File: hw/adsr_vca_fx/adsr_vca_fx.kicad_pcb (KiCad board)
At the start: 4 copper layers, 87 x 89.5 mm, 110 parts, among them J1 Conn_01x03, J10 VCA2 Extern, J11 Conn_01x04, J2 Conn_02x02_Odd_Even, J3 Conn_02x02_Odd_Even, J4 Audio Input, J5 Audio Output, J6 Conn_02x05_Odd_Even, J7 Envelope2 Extern, J8 Envelope1 Extern, J9 VCA1 Extern, Q1 HX2301A, SW1 SW_Push, U1 TL972, U2 MCP603-xCH, U3 STM32L432KBUx, U4 LM13700, U5 TL972, U6 TPS563200, U7 SE8233X2, U8 TPS60403, U9 TPS60403

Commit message: tidied up layout
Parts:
- removed JP2: SolderJumper_3_Bridged12, Jumper:SolderJumper-3_P1.3mm_Bridged12_Pad1.0x1.5mm
- added J12: Conn_01x03, Connector_PinHeader_2.54mm:PinHeader_1x03_P2.54mm_Vertical, F.Cu at (175.9, 78.1)
- JP1: footprint Connector_PinSocket_2.54mm:PinSocket_1x02_P2.54mm_Vertical -> Connector_PinHeader_2.54mm:PinHeader_1x02_P2.54mm_Vertical
- moved J4 18.7 mm to (146.6, 129.7), turned to 90 degrees
- moved RV4 12.6 mm to (192.3, 121.1), turned to -90 degrees
- moved RV14 12.5 mm to (123.2, 136.5), turned to -90 degrees
- moved RV11 12.5 mm to (123.2, 85.1), turned to -90 degrees
- moved RV12 12.5 mm to (123.2, 119.4), turned to -90 degrees
- moved RV13 12.5 mm to (123.2, 102.2), turned to -90 degrees
- moved RV2 12.5 mm to (192.3, 85.6), turned to -90 degrees
- moved RV3 12.5 mm to (192.3, 103.2), turned to -90 degrees
- moved R2 11.6 mm to (189.7, 91.9)
- moved R6 9.85 mm to (175.9, 81.3)
- moved TP5 7.67 mm to (142.2, 104.8)
- moved J7 6.66 mm to (134.6, 105.2), turned to 90 degrees
- moved TP8 5.84 mm to (163.0, 143.0)
- moved R4 5.04 mm to (188.8, 124.0), turned to 180 degrees
- moved J8 4.30 mm to (177.8, 105.4)
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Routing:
- net +3.3V: track 278.8 -> 251.3 mm, vias 9 -> 8
- net /AudioOutput/audio_in1: track 47.2 -> 63.8 mm
- net /AudioOutput/audio_in2: track 44.4 -> 57.6 mm
- net Net-(R3-Pad1): track 2.67 -> 12.5 mm
- net /AudioInput/audio_out: track 66.5 -> 75.8 mm
- net /ADSRPots/env_in.decay: track 62.6 -> 53.6 mm
- net /ADSRPots/env_in.attack: track 48.6 -> 39.7 mm
- net /ADSRPots/env_in.sustain: track 77.7 -> 69.0 mm
- net /ADSRPots/env_in.release: track 93.6 -> 85.2 mm
- net /EnvelopeGenerator/boot0: track 10.8 -> 18.8 mm, vias 1 -> 0
- net Net-(J4-Pin_2): track 28.4 -> 36.3 mm
- net Net-(U4C--): track 27.4 -> 22.8 mm
- net Net-(U1B--): track 65.4 -> 69.9 mm
- net /EnvelopeGenerator/reset: track 39.3 -> 43.4 mm
- net Net-(J8-Pin_2): track 37.5 -> 34.1 mm
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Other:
- board text removed: "+12V"
- board text removed: "+5V"
- board text removed: "-5V"
- board text removed: "DETECT"
- board text removed: "INPUT"
- board text removed: "INPUT GAIN"
- board text removed: "OUTPUT"
- board text removed: "PEAK"
- board text removed: "VCA1"
- board text removed: "VCA1 ENV OUT"
- board text removed: "VCA1 GAIN"
- board text removed: "VCA1 OFFSET"
- board text removed: "VCA2"
- board text removed: "VCA2 ENV OUT"
- board text removed: "VCA2 GAIN"
- board text removed: "VCA2 OFFSET"

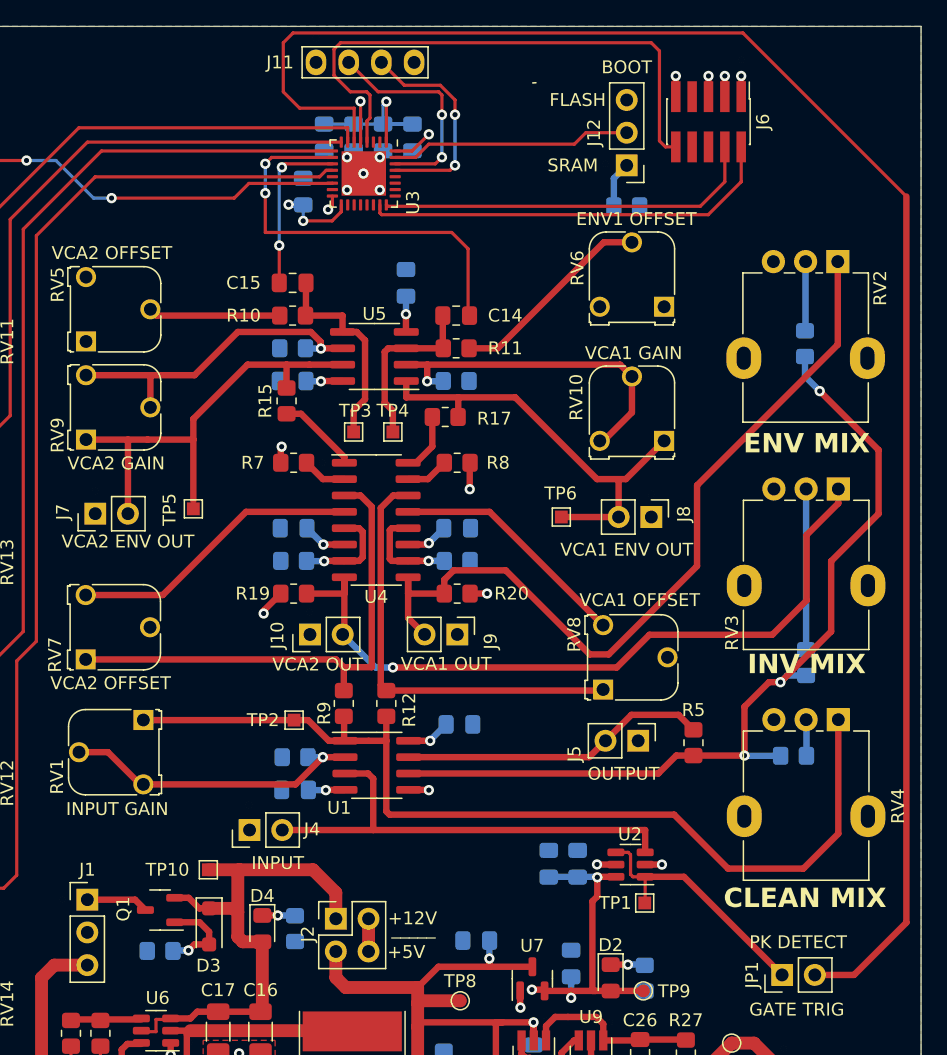
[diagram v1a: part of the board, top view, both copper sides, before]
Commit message: updated layout
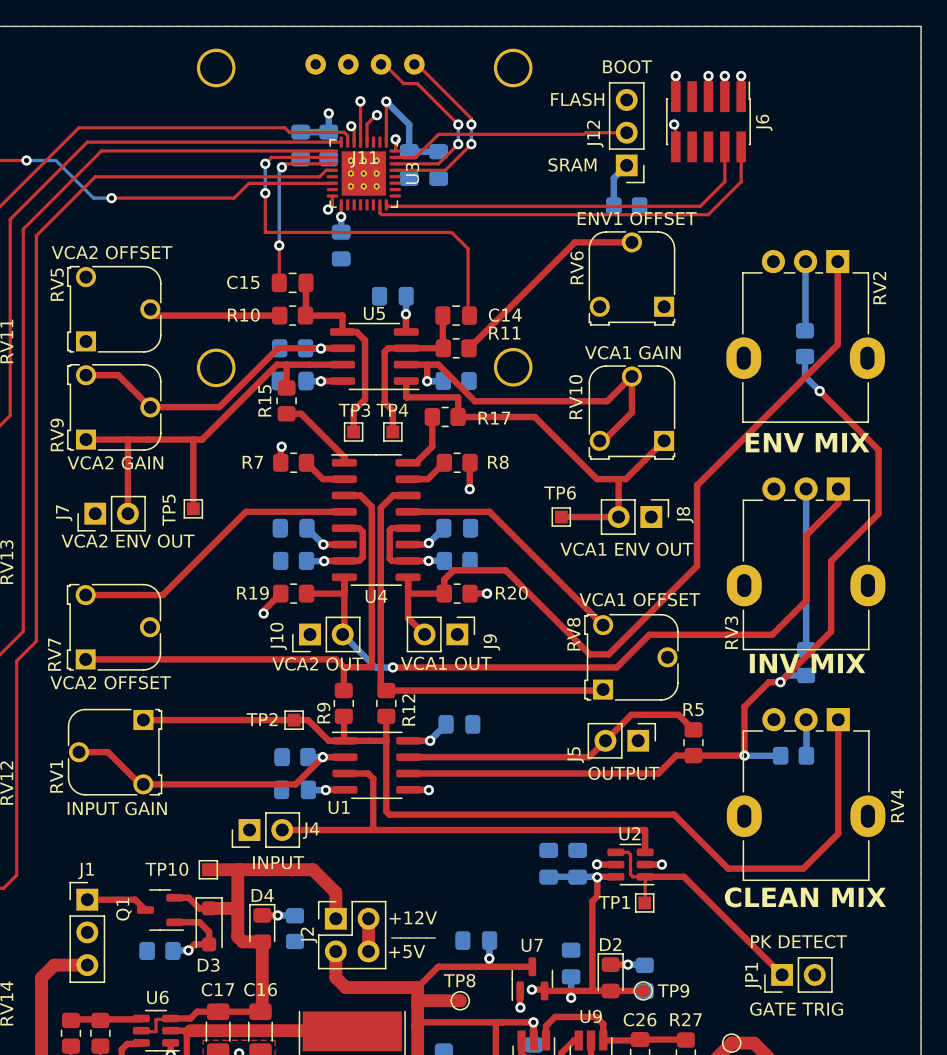
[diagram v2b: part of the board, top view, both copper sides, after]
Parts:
- J11: footprint 128x64_0_96InchOLED:128x64_0_96InchOLED -> SSD1306_0.96_Oled:SSD1306_0.96_Oled_no_courtyard_no_silkscreen
- U3: footprint Package_DFN_QFN:QFN-32-1EP_5x5mm_P0.5mm_EP3.45x3.45mm -> Package_DFN_QFN:QFN-32-1EP_5x5mm_P0.5mm_EP3.45x3.45mm_ThermalVias
- moved J11 18.8 mm to (142.6, 94.5)
- moved C7 9.15 mm to (161.3, 78.1)
- moved C8 6.53 mm to (152.8, 76.6)
- moved C9 6.43 mm to (150.6, 76.6)
- moved C6 5.13 mm to (153.7, 84.3), turned to -90 degrees
- moved C5 4.82 mm to (159.0, 78.1)
- moved C13 1.45 mm to (157.7, 88.3), turned to 0 degrees
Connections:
- J11 pad 2: /EnvelopeGenerator/displaybus.sda -> +3.3V
- J11 pad 3: /EnvelopeGenerator/displaybus.scl -> /EnvelopeGenerator/displaybus.sda
- J11 pad 4: +3.3V -> /EnvelopeGenerator/displaybus.scl
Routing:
- net /EnvelopeGenerator/peak_detect_gatecv: track 131.6 -> 91.6 mm, vias 0 -> 1
- net /EnvelopeGenerator/reset: track 43.4 -> 27.6 mm, vias 0 -> 2
- net +3.3V: track 251.3 -> 260.4 mm
- net VDDA: track 147.5 -> 144.2 mm
- net GND: track 36.2 -> 33.9 mm, vias 23 -> 18
- net /EnvelopeGenerator/displaybus.sda: track 17.0 -> 15.0 mm
- net /EnvelopeGenerator/displaybus.scl: track 16.8 -> 15.0 mm
- net Net-(U5B--): track 25.8 -> 24.0 mm
- net Net-(U5A--): track 26.7 -> 28.3 mm
- net Net-(J7-Pin_2): track 35.6 -> 34.6 mm
- net Net-(J8-Pin_2): track 34.1 -> 33.4 mm

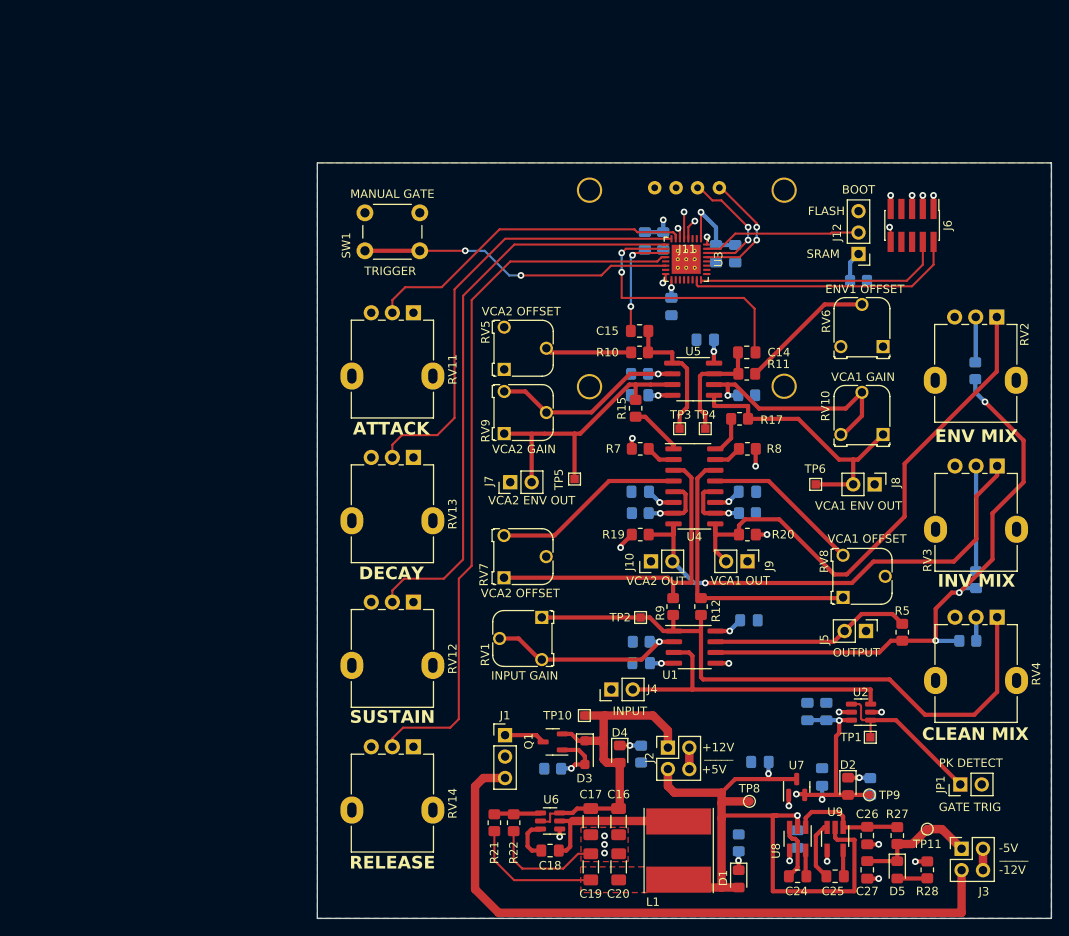
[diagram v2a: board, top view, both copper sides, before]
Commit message: updated layout
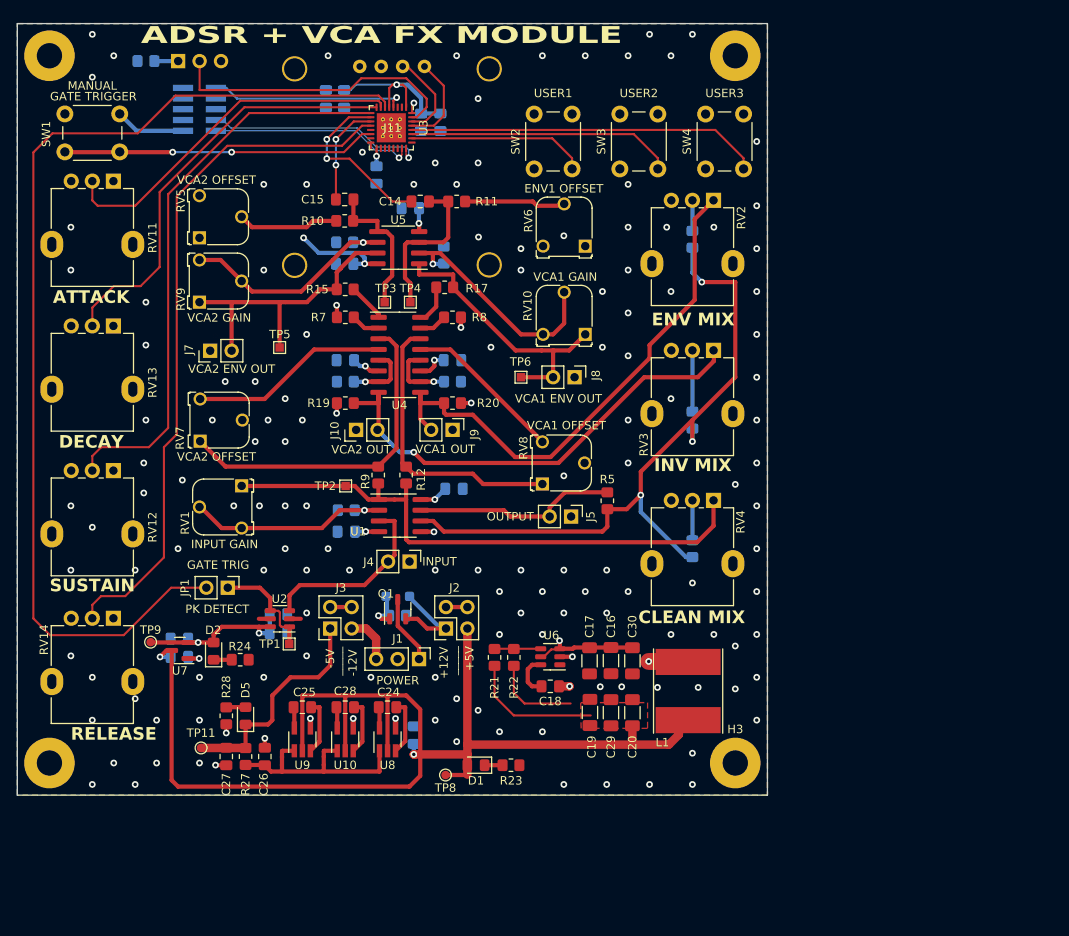
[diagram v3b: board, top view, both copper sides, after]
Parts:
- removed D4: RED, LED_SMD:LED_0805_2012Metric_Pad1.15x1.40mm_HandSolder
- removed R26: 2K2, Resistor_SMD:R_0805_2012Metric_Pad1.20x1.40mm_HandSolder
- removed TP10: TestPoint, TestPoint:TestPoint_Pad_1.0x1.0mm
- added C28: 1uf, Capacitor_SMD:C_0805_2012Metric_Pad1.18x1.45mm_HandSolder, F.Cu at (115.1, 131.8)
- added C29: 22uF, Resistor_SMD:R_1206_3216Metric_Pad1.30x1.75mm_HandSolder, F.Cu at (146.6, 132.5)
- added C30: 100nF, Resistor_SMD:R_1206_3216Metric_Pad1.30x1.75mm_HandSolder, F.Cu at (149.1, 126.3)
- added H1: MountingHole, MountingHole:MountingHole_3mm_Pad, F.Cu at (161.3, 54.6)
- added H2: MountingHole, MountingHole:MountingHole_3mm_Pad, F.Cu at (80.0, 54.6)
- added H3: MountingHole, MountingHole:MountingHole_3mm_Pad, F.Cu at (161.3, 138.4)
- added H4: MountingHole, MountingHole:MountingHole_3mm_Pad, F.Cu at (80.0, 138.4)
- added NT2: NetTie_2, NetTie:NetTie-2_SMD_Pad0.5mm, F.Cu at (107.6, 138.2)
- added SW2: SW_Push, Button_Switch_THT:SW_PUSH_6mm, F.Cu at (137.4, 68.0)
- added SW3: SW_Push, Button_Switch_THT:SW_PUSH_6mm, F.Cu at (147.6, 68.0)
- added SW4: SW_Push, Button_Switch_THT:SW_PUSH_6mm, F.Cu at (157.8, 68.0)
- added U10: TPS60403, Package_TO_SOT_SMD:SOT-23-5_HandSoldering, F.Cu at (115.1, 135.6)
- C16, C17: value 10uF 20V X5R -> 10uF
- C19, C20: value 22uF 10V X5R -> 22uF
- D3, J12, J6: moved to B.Cu
- R23, R24: moved to F.Cu
- moved JP1 89.9 mm to (101.1, 117.7), turned to -90 degrees
- moved R6 88.4 mm to (91.4, 55.2), turned to 180 degrees
- moved TP9 87.1 mm to (92.0, 124.1), turned to 0 degrees
- moved TP11 86.6 mm to (98.0, 136.6), turned to 180 degrees
- moved J6 85.6 mm to (97.8, 61.0), turned to 0 degrees
- moved R28 85.1 mm to (101.0, 132.8), turned to -90 degrees
- moved J12 83.8 mm to (95.3, 55.2), turned to -90 degrees
- moved D5 79.4 mm to (103.3, 132.8), turned to 90 degrees
- moved J3 79.2 mm to (113.3, 122.5), turned to 90 degrees
- moved C22 77.9 mm to (95.4, 123.7), turned to 180 degrees
- moved R27 77.8 mm to (103.3, 137.7), turned to 90 degrees
- moved C27 77.1 mm to (101.0, 137.7)
- moved D2 76.9 mm to (99.5, 125.2), turned to 90 degrees
- moved R24 76.2 mm to (102.6, 126.2), turned to 0 degrees
- moved U7 74.9 mm to (95.5, 125.1), turned to 180 degrees
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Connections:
- C26 pad 1: Net-(U9-OUT) -> Net-(U8-OUT)
- NT1 pad 1: Net-(U8-OUT) -> Net-(U10-OUT)
- NT1 pad 2: Net-(U9-OUT) -> Net-(U8-OUT)
- R27 pad 1: Net-(U9-OUT) -> Net-(U8-OUT)
- U3 pad 26: unconnected-(U3-PB3-Pad26) -> /EnvelopeGenerator/user_btn1
- U3 pad 27: unconnected-(U3-PB4-Pad27) -> /EnvelopeGenerator/user_btn2
- U3 pad 28: unconnected-(U3-PB5-Pad28) -> /EnvelopeGenerator/user_btn3
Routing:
- net VSSA: track 231.1 -> 134.3 mm
- net VSS: track 80.0 -> 5.83 mm
- net /PowerSupply/+5V: track 100.6 -> 165.0 mm
- net /EnvelopeGenerator/user_btn3: track 0.00 -> 48.5 mm
- net /EnvelopeGenerator/user_btn2: track 0.00 -> 38.1 mm
- net /EnvelopeGenerator/peak_detect_gatecv: track 91.6 -> 124.3 mm, vias 1 -> 0
- net /EnvelopeGenerator/user_btn1: track 0.00 -> 27.7 mm
- net Net-(U8-OUT): track 2.12 -> 20.2 mm
- net /EnvelopeGenerator/boot0: track 18.8 -> 35.2 mm
- net VDDA: track 144.2 -> 129.9 mm, vias 5 -> 6
- net Net-(J4-Pin_2): track 36.3 -> 22.1 mm
- net Net-(U1B--): track 69.9 -> 82.4 mm
- net +3.3V: track 260.4 -> 272.8 mm, vias 8 -> 4
- net /PowerSupply/-5V: track 14.9 -> 27.2 mm
- net /EnvelopeGenerator/adsr_env_out1: track 32.3 -> 20.7 mm
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- added copper zone on In2.Cu, net GND
- removed copper zone on In1.Cu, net GND
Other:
- board size 87 x 89.5 mm -> 88.9 x 91.4 mm
- board text added: "ADSR + VCA FX MODULE"

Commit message: completed layout
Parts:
- removed TP11, TP8, TP9: TestPoint, TestPoint:TestPoint_Pad_D1.0mm
- Q1: value HX2301A -> HX2301A PMOS
- moved R24 6.55 mm to (109.2, 126.2)
- moved D2 4.29 mm to (103.6, 126.2), turned to 180 degrees
- moved R28 3.93 mm to (97.3, 134.3), turned to 180 degrees
- moved TP1 2.76 mm to (108.4, 121.6)
- moved U2 2.76 mm to (107.3, 118.6)
- moved C3 2.76 mm to (107.1, 120.3)
- moved C4 2.76 mm to (107.1, 118.0)
- moved D5 2.45 mm to (101.3, 134.3), turned to 180 degrees
- moved J12 1.91 mm to (95.3, 57.1)
- moved J6 1.91 mm to (97.8, 62.9)
- moved R6 1.91 mm to (91.4, 57.1)
- moved J1 1.04 mm to (123.8, 127.2)
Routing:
- net +3.3V: track 272.8 -> 278.3 mm
- net /PowerSupply/+5V: track 165.0 -> 161.3 mm
- net /PowerSupply/-5V: track 27.2 -> 24.8 mm
- net Net-(J4-Pin_2): track 22.1 -> 19.9 mm
- net /AudioInput/peak_detect_out: track 13.1 -> 11.1 mm
- net /EnvelopeGenerator/boot0: track 35.2 -> 33.3 mm
- net Net-(D2-K): track 2.31 -> 3.51 mm
- net /EnvelopeGenerator/manual_gate_cv: track 37.3 -> 38.3 mm
- net /EnvelopeGenerator/swdio: track 24.3 -> 25.1 mm
- net GND: track 24.5 -> 24.8 mm, vias 145 -> 180
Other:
- board text added: "+3.3V"
- board text added: "+5V"
- board text added: "+9/ +12V"
- board text added: "-5V"
- board text added: "NC/ -12V"
- board text added: "RevA 14/23"
